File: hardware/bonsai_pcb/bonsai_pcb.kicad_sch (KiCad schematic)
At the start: 5 parts, among them J1 Audio Amp Conn, J2 B+ Wire, J3 PH2.0 Battery Connector, SW1 BT1, U1 XIAO-ESP32-S3-SMD

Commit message: Update PCB, schematic, and STEP model
Co-Authored-By: Claude Sonnet 5 <noreply@anthropic.com>
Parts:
- removed J1: Audio Amp Conn, Connector_PinSocket_2.54mm:PinSocket_1x07_P2.54mm_Vertical, symbol Connector:Conn_01x07_Socket
- removed J3: PH2.0 Battery Connector, Connector_JST:JST_PH_S2B-PH-K_1x02_P2.00mm_Horizontal, symbol Connector:Conn_01x02_Socket
- removed SW1: BT1, Button_Switch_THT:SW_PUSH_6mm, symbol Switch:SW_Push
- added C1: 10uF, JLCPCB_Capacitors:C0402, symbol JLCPCB_Capacitors:CL05A106MQ5NUNC
- added C2: 100nF, JLCPCB_Capacitors:C0402, symbol JLCPCB_Capacitors:CL05B104KO5NNNC
- added CN2: S2B-PH-SM4-TB, JLCPCB_Connectors:CONN-SMD_P2.00_S2B-PH-SM4-TB-LF-SN, symbol JLCPCB_Connectors:S2B-PH-SM4-TB
- added J1, J3: Conn_01x01_Socket, Connector_Wire:SolderWirePad_1x01_SMD_2x4mm, symbol Connector:Conn_01x01_Socket
- added SW1: TS-1102N-5516, JLCPCB_Switches:SW-TH_TS-1102N-5516, symbol JLCPCB_Switches:TS-1102N-5516
- added U2: MAX98357AETE+T, JLCPCB_Amplifiers:TQFN-16_L3.0-W3.0-P0.50-BL-EP1.5, symbol JLCPCB_Amplifiers:MAX98357AETE+T
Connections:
- net BLCK: now also U1.2 (GPIO2_A1_D1), U2.16 (BCLK); no longer U1.10 (GPIO8_A9_D9_MISO)
- net BT1: now also U1.11 (GPIO9_A10_D10_MOSI), SW1.1; no longer U1.1 (GPIO1_A0_D0)
- net DIN: now also U1.1 (GPIO1_A0_D0), U2.1 (DIN); no longer U1.11 (GPIO9_A10_D10_MOSI)
- net GND: now also U1.34 (PAD), C1.2, C2.2, CN2.1, SW1.2, U2.11 (GND), U2.15 (GND), U2.17 (EP), U2.2 (GAIN_SLOT), U2.3 (GND)
- net LRC: now also U1.3 (GPIO3_A2_D2), U2.14 (LRCLK); no longer U1.9 (GPIO7_A8_D8_SCK)
- net SD: now also U1.10 (GPIO8_A9_D9_MISO), U2.4 (~{SD_MODE}); no longer U1.8 (GPIO44_D7_RX)
- net VIN: now also C1.1, C2.1, U2.7 (VDD), U2.8 (VDD)
- net at J2.1 (Pin_1): now also CN2.2
- new net OUTN: J1.1 (Pin_1), U2.10 (OUTN)
- new net OUTP: J3.1 (Pin_1), U2.9 (OUTP)
- no-connect marks 17 -> 18
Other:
- note removed: "MAX98357 Pin Header"
- moved on the sheet: J2, U1

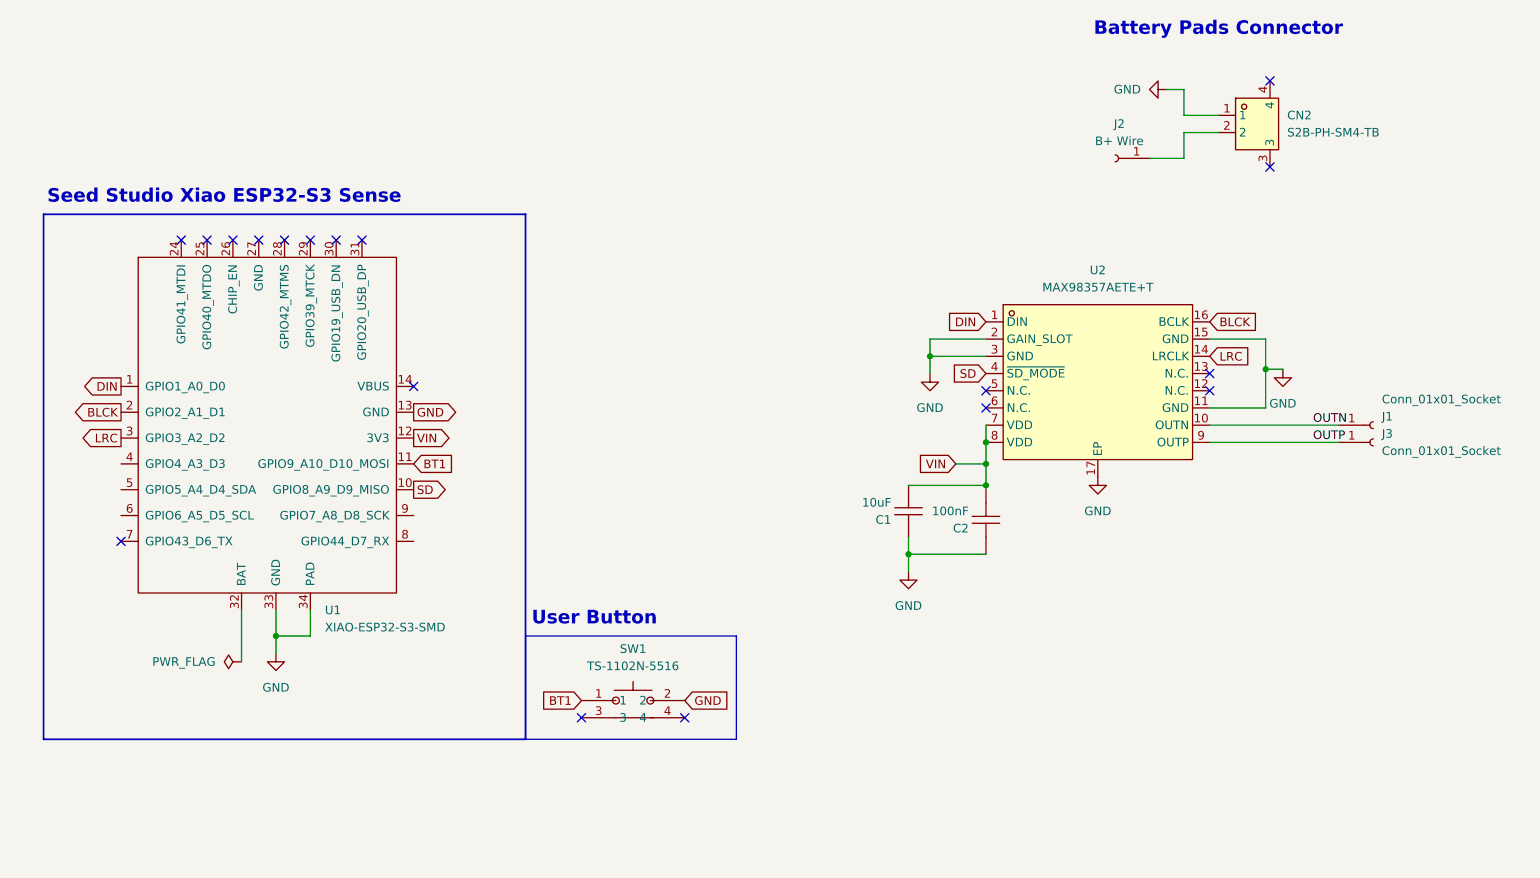
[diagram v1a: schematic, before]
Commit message: Redraw the board with the tactile switch and the logo silkscreen
Brings in the JLCPCB tactile-switch symbol/footprint/3D model, adds the
logo footprint on the silkscreen, and reworks the schematic and layout
around them.

Co-Authored-By: Claude Opus 5 <noreply@anthropic.com>
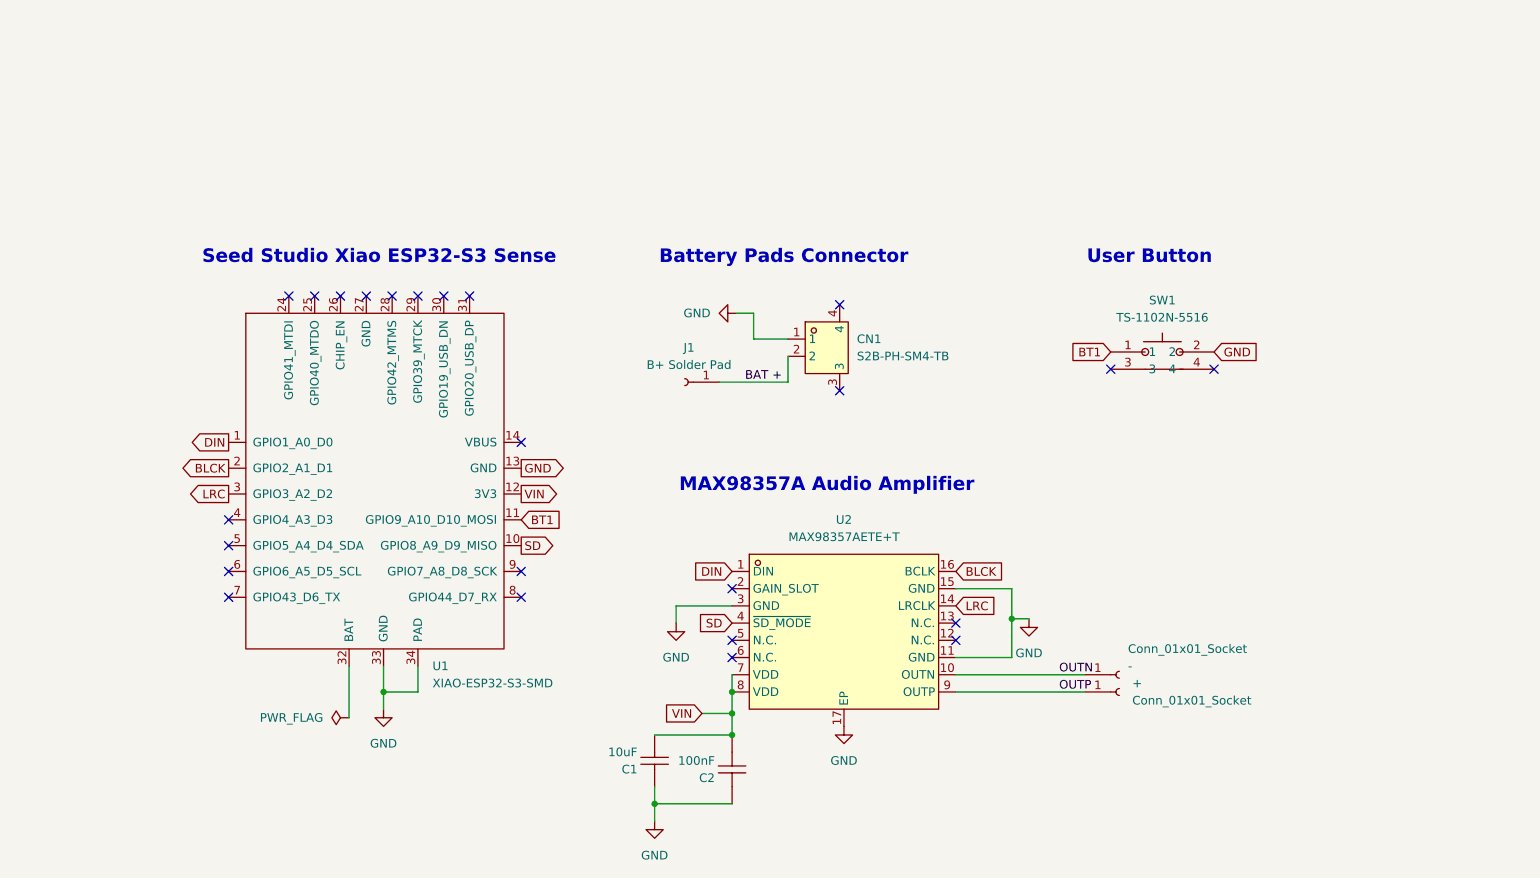
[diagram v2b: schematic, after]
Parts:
- J1: renamed from J2; value B+ Wire -> B+ Solder Pad
- renumbered J3 to +, J1 to -, CN2 to CN1
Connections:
- net GND: no longer U2.2 (GAIN_SLOT)
- net BAT +: now reaches CN1.2, J1.1 (Pin_1)
- no-connect marks 18 -> 24
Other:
- note added: "MAX98357A Audio Amplifier"
- company: (none) -> Biel Vázquez Mata
- title: (none) -> Bonsai PCB
- moved on the sheet: +, -, C1, C2, CN1, J1, SW1, U1, U2
